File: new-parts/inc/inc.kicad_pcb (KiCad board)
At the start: 2 copper layers, 68.6 x 115.6 mm, 20 parts, among them J1 BHR-10-VUA, J2 BHR-10-VUA, J3 Conn_01x02, J4 Conn_01x01, K1 J104D2C12VDC.15S, K2 J104D2C12VDC.15S, K3 J104D2C12VDC.15S, K4 J104D2C12VDC.15S, K5 J104D2C12VDC.15S, K6 J104D2C12VDC.15S, K7 J104D2C12VDC.15S, K8 J104D2C12VDC.15S

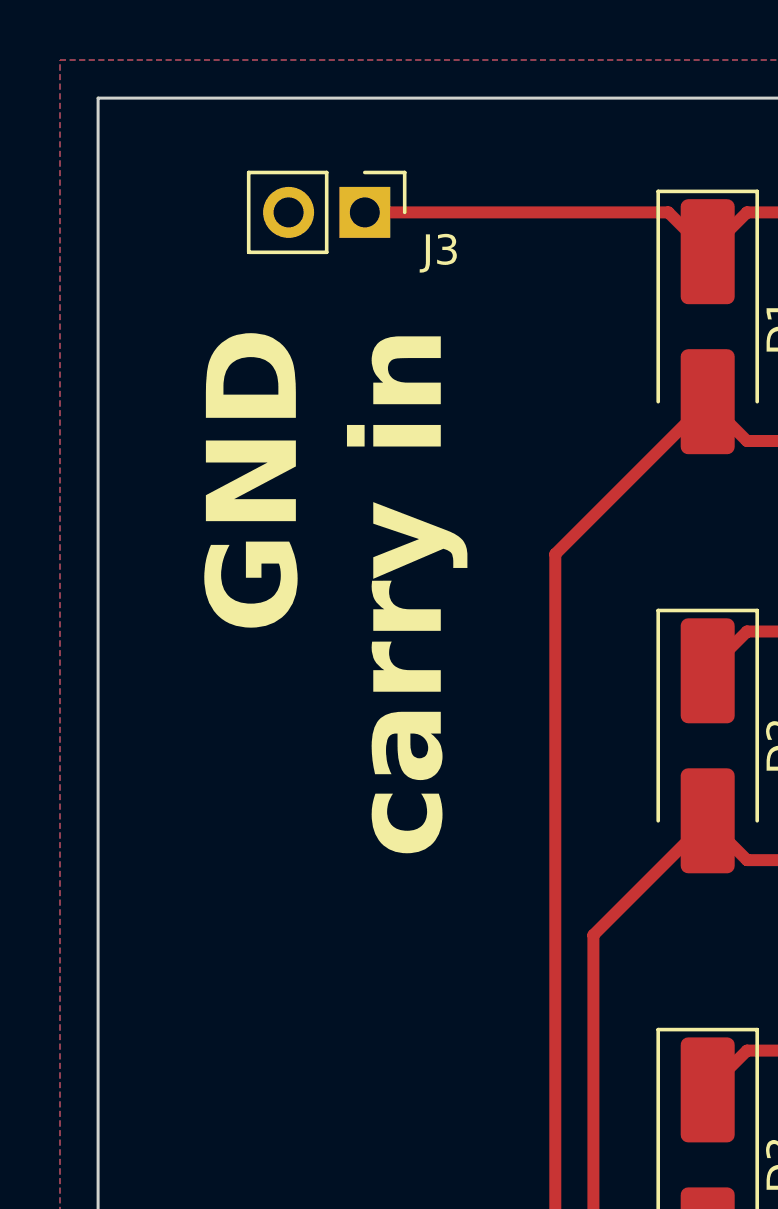
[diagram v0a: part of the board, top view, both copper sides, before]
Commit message: Change all two-pin headers for control + ground to control only.
This is to prevent accidental short circuits when they are plugged in the
wrong way.
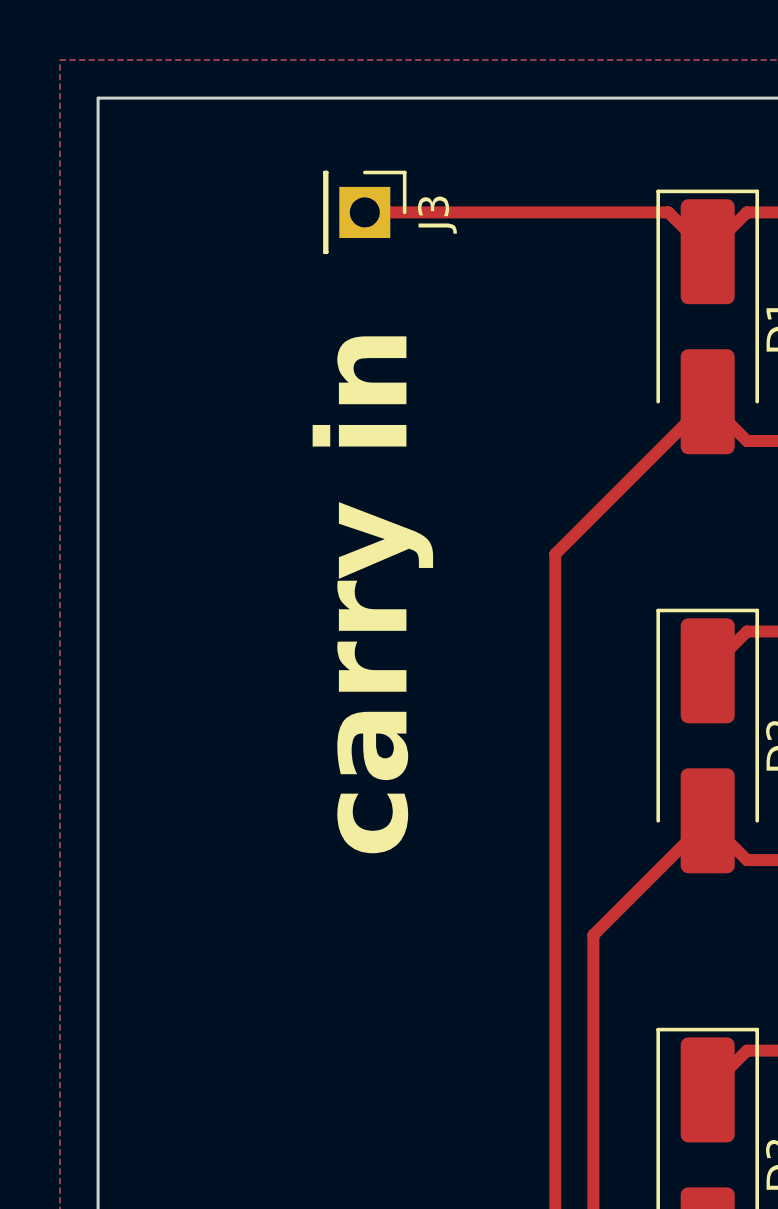
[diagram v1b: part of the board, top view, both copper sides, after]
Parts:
- J3: footprint Connector_PinHeader_2.54mm:PinHeader_1x02_P2.54mm_Vertical -> Connector_PinHeader_2.54mm:PinHeader_1x01_P2.54mm_Vertical
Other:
- board text added: "carry in"
- board text removed: "GND carry in"
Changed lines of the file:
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@@
   (net 26 "Net-(D1-A2)")
   (net 27 "Net-(J4-Pin_1)")
-  (footprint "Connector_PinHeader_2.54mm:PinHeader_1x02_P2.54mm_Vertical" (layer "F.Cu")
+  (footprint "Connector_PinHeader_2.54mm:PinHeader_1x01_P2.54mm_Vertical" (layer "F.Cu")
     (at 125.73 45.72 -90)
-    (descr "Through hole straight pin header, 1x02, 2.54mm pitch, single row")
-    (tags "Through hole pin header THT 1x02 2.54mm single row")
-    (property "Sheetfile" "inc.kicad_sch")
-    (property "Sheetname" "")
-    (property "ki_description" "Generic connector, single row, 01x02, script generated (kicad-library-utils/schlib/autogen/connector/)")
+    (descr "Through hole straight pin header, 1x01, 2.54mm pitch, single row")
+    (tags "Through hole pin header THT 1x01 2.54mm single row")
+    (property "Sheetfile" "inc.kicad_sch")
+    (property "Sheetname" "")
+    (property "ki_description" "Generic connector, single row, 01x01, script generated (kicad-library-utils/schlib/autogen/connector/)")
     (property "ki_keywords" "connector")
     (attr through_hole)
-    (fp_text reference "J3" (at 1.27 -2.54 -180) (layer "F.SilkS")
-        (effects (font (size 1 1) (thickness 0.15)))
-    )
-    (fp_text value "Conn_01x02" (at 0 4.87 90) (layer "F.Fab")
-        (effects (font (size 1 1) (thickness 0.15)))
-    )
-    (fp_text user "${REFERENCE}" (at 0 1.27) (layer "F.Fab")
+    (fp_text reference "J3" (at 0 -2.33 -90) (layer "F.SilkS")
+        (effects (font (size 1 1) (thickness 0.15)))
+    )
+    (fp_text value "Conn_01x02" (at 0 2.33 -90) (layer "F.Fab")
+        (effects (font (size 1 1) (thickness 0.15)))
+    )
+    (fp_text user "${REFERENCE}" (at 0 0) (layer "F.Fab")
         (effects (font (size 1 1) (thickness 0.15)))
     )
@@
     (fp_line (start -1.33 0) (end -1.33 -1.33)
       (stroke (width 0.12) (type solid)) (layer "F.SilkS"))
-    (fp_line (start -1.33 1.27) (end -1.33 3.87)
+    (fp_line (start -1.33 1.27) (end -1.33 1.33)
       (stroke (width 0.12) (type solid)) (layer "F.SilkS"))
     (fp_line (start -1.33 1.27) (end 1.33 1.27)
       (stroke (width 0.12) (type solid)) (layer "F.SilkS"))
-    (fp_line (start -1.33 3.87) (end 1.33 3.87)
-      (stroke (width 0.12) (type solid)) (layer "F.SilkS"))
-    (fp_line (start 1.33 1.27) (end 1.33 3.87)
-      (stroke (width 0.12) (type solid)) (layer "F.SilkS"))
-    (fp_line (start -1.8 -1.8) (end -1.8 4.35)
-      (stroke (width 0.05) (type solid)) (layer "F.CrtYd"))
-    (fp_line (start -1.8 4.35) (end 1.8 4.35)
+    (fp_line (start -1.33 1.33) (end 1.33 1.33)
+      (stroke (width 0.12) (type solid)) (layer "F.SilkS"))
+    (fp_line (start 1.33 1.27) (end 1.33 1.33)
+      (stroke (width 0.12) (type solid)) (layer "F.SilkS"))
+    (fp_line (start -1.8 -1.8) (end -1.8 1.8)
+      (stroke (width 0.05) (type solid)) (layer "F.CrtYd"))
+    (fp_line (start -1.8 1.8) (end 1.8 1.8)
       (stroke (width 0.05) (type solid)) (layer "F.CrtYd"))
     (fp_line (start 1.8 -1.8) (end -1.8 -1.8)
       (stroke (width 0.05) (type solid)) (layer "F.CrtYd"))
-    (fp_line (start 1.8 4.35) (end 1.8 -1.8)
+    (fp_line (start 1.8 1.8) (end 1.8 -1.8)
       (stroke (width 0.05) (type solid)) (layer "F.CrtYd"))
     (fp_line (start -1.27 -0.635) (end -0.635 -1.27)
       (stroke (width 0.1) (type solid)) (layer "F.Fab"))
-    (fp_line (start -1.27 3.81) (end -1.27 -0.635)
+    (fp_line (start -1.27 1.27) (end -1.27 -0.635)
       (stroke (width 0.1) (type solid)) (layer "F.Fab"))
     (fp_line (start -0.635 -1.27) (end 1.27 -1.27)
       (stroke (width 0.1) (type solid)) (layer "F.Fab"))
-    (fp_line (start 1.27 -1.27) (end 1.27 3.81)
-      (stroke (width 0.1) (type solid)) (layer "F.Fab"))
-    (fp_line (start 1.27 3.81) (end -1.27 3.81)
+    (fp_line (start 1.27 -1.27) (end 1.27 1.27)
+      (stroke (width 0.1) (type solid)) (layer "F.Fab"))
+    (fp_line (start 1.27 1.27) (end -1.27 1.27)
       (stroke (width 0.1) (type solid)) (layer "F.Fab"))
     (pad "1" thru_hole rect (at 0 0 270) (size 1.7 1.7) (drill 1) (layers "*.Cu" "*.Mask")
       (net 25 "Net-(D1-A1)") (pinfunction "Pin_1") (pintype "passive"))
-    (pad "2" thru_hole oval (at 0 2.54 270) (size 1.7 1.7) (drill 1) (layers "*.Cu" "*.Mask")
-      (net 16 "GND") (pinfunction "Pin_2") (pintype "passive"))
-    (model "${KICAD6_3DMODEL_DIR}/Connector_PinHeader_2.54mm.3dshapes/PinHeader_1x02_P2.54mm_Vertical.wrl"
+    (model "${KICAD6_3DMODEL_DIR}/Connector_PinHeader_2.54mm.3dshapes/PinHeader_1x01_P2.54mm_Vertical.wrl"
       (offset (xyz 0 0 0))
       (scale (xyz 1 1 1))
@@
     (effects (font (size 3 3) (thickness 0.6) bold) (justify left bottom))
   )
-  (gr_text "GND\ncarry in" (at 124.46 49.53 90) (layer "F.SilkS")
+  (gr_text "carry in" (at 125.73 49.53 90) (layer "F.SilkS")
     (effects (font (size 3 3) (thickness 0.6) bold) (justify right))
   )

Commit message: Add placeholders for JLC order number.
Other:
- board text added: "JLCJLCJLCJLC"
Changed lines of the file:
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@@
   (gr_line (start 116.84 41.91) (end 185.42 41.91)
     (stroke (width 0.1) (type default)) (layer "Edge.Cuts"))
+  (gr_text "JLCJLCJLCJLC" (at 183.896 155.956) (layer "B.SilkS")
+    (effects (font (size 1 1) (thickness 0.15)) (justify left bottom mirror))
+  )
   (gr_text "A in" (at 119.38 85.09) (layer "F.SilkS")
     (effects (font (size 3 3) (thickness 0.6) bold) (justify left bottom))

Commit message: Add a "title" label to all parts.
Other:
- board text added: "vis vitalis incrementer"
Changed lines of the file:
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@@
   (gr_line (start 116.84 41.91) (end 185.42 41.91)
     (stroke (width 0.1) (type default)) (layer "Edge.Cuts"))
+  (gr_text "vis vitalis\nincrementer" (at 172.466 147.32 270) (layer "B.SilkS")
+    (effects (font (size 3 3) (thickness 0.6) bold) (justify left bottom mirror))
+  )
   (gr_text "JLCJLCJLCJLC" (at 183.896 155.956) (layer "B.SilkS")
     (effects (font (size 1 1) (thickness 0.15)) (justify left bottom mirror))
